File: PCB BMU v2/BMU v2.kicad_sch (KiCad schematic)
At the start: 32 parts, among them J11 Screw_Terminal_01x01, J12 Screw_Terminal_01x01, J3 Conn_01x02_Pin, U8 VPS8505, U9 MCP16331T-E/CH

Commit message: update code
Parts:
- removed JP1: SolderJumper_2_Open, Jumper:SolderJumper-2_P1.3mm_Open_RoundedPad1.0x1.5mm, symbol Jumper:SolderJumper_2_Open
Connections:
- net GND_BATT is gone; now on net GND: C12.2, C13.2, C19.2, C20.2, D1.2 (A), R25.2, U9.2 (GND)
- net batteries1/-BATT OUT is gone; now on net GND: H11.1, J12.1 (Pin_1)
- net VCC: now also U8.5 (EN)
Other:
- sheet batteries1 ports: added +BATT OUT; removed +BATT_OUT, -BATT OUT, GND_BATT
- sheet batteries2 ports: added +BATT OUT; removed +BATT_OUT, -BATT OUT
- sheet batteries3 ports: added +BATT OUT; removed +BATT_OUT, -BATT OUT
- sheet batteries4 ports: added +BATT OUT; removed +BATT_OUT, -BATT OUT
- moved on the sheet: H12, U8

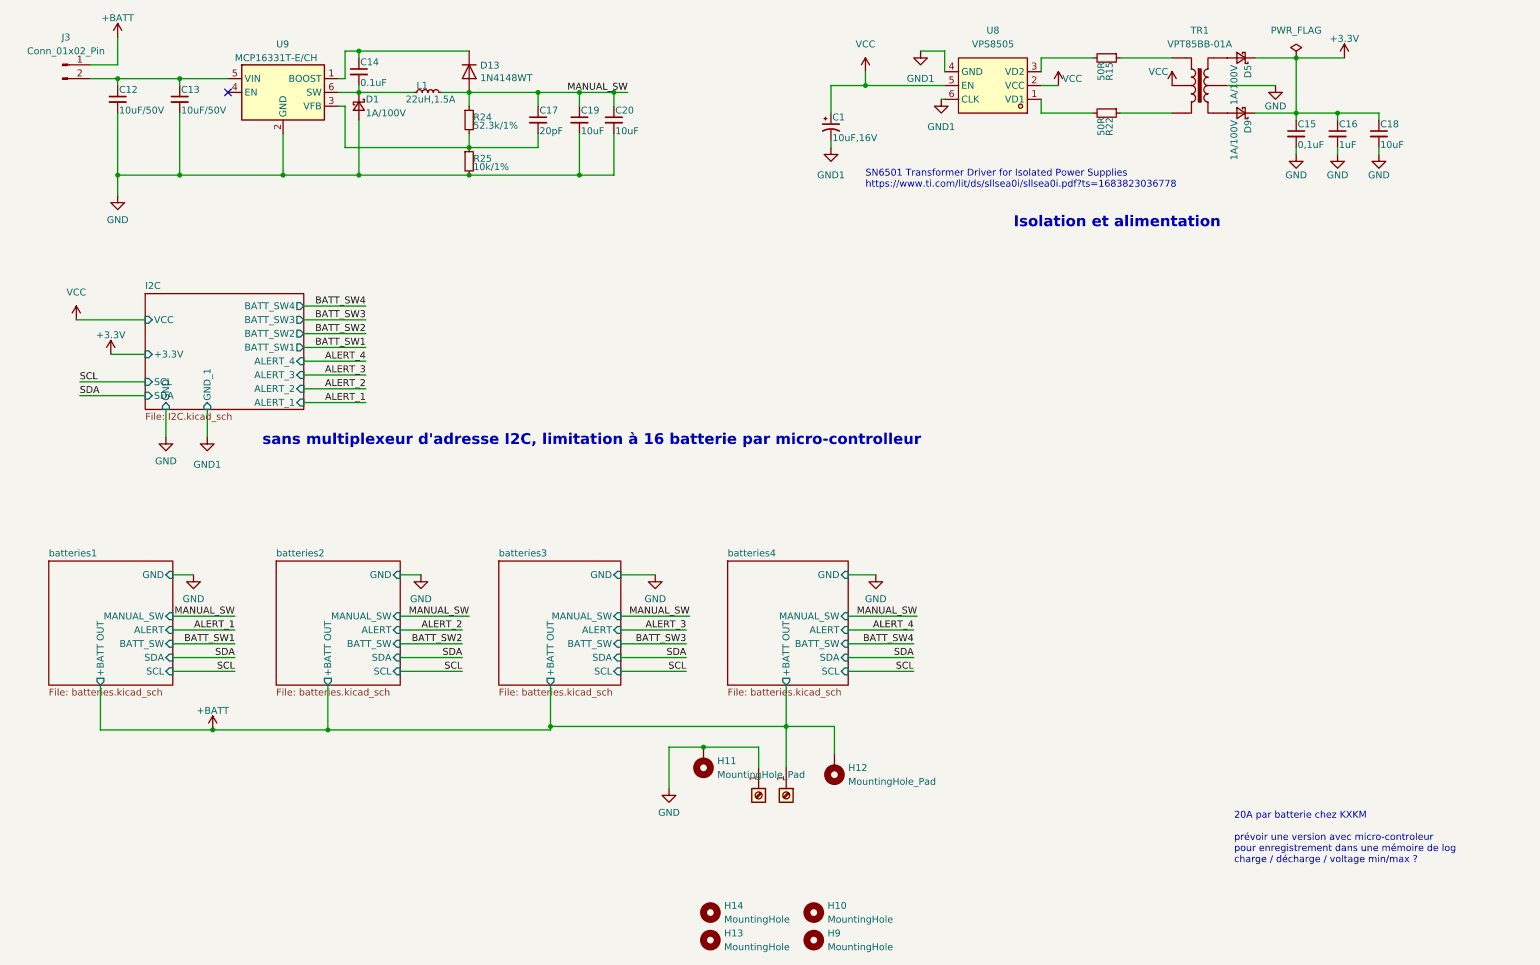
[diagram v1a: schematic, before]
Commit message: add Ampère/Houre calculation
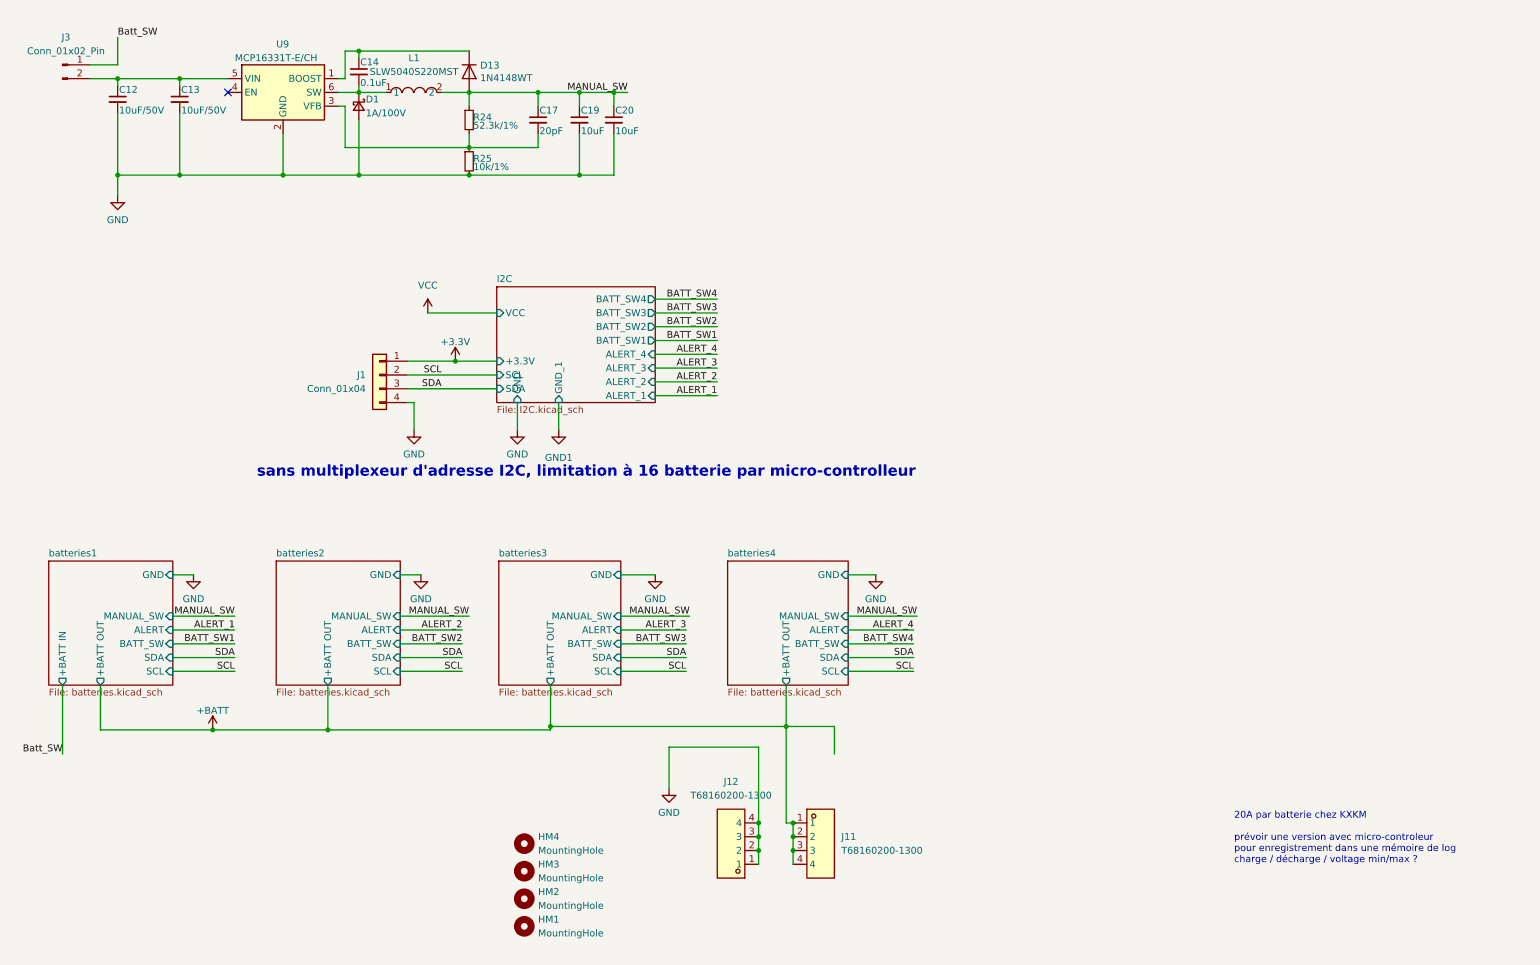
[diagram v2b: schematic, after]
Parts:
- removed C1: 10uF,16V, Capacitor_SMD:CP_Elec_8x10, symbol KXKM_ESP32_battery_management_board-rescue:CP1_Small-Device
- removed C15: 0,1uF, Capacitor_SMD:C_0805_2012Metric, symbol Device:C_Small
- removed C16: 1uF, Capacitor_SMD:C_0805_2012Metric, symbol Device:C_Small
- removed C18: 10uF, Capacitor_SMD:C_0805_2012Metric, symbol Device:C_Small
- removed D5, D9: 1A/100V, Diode_SMD:D_SMA, symbol Device:D_Schottky_Small
- removed H10, H13, H14: MountingHole, MountingHole:MountingHole_3.2mm_M3_DIN965, symbol Mechanical:MountingHole
- removed H11, H12: MountingHole_Pad, MountingHole:MountingHole_3.2mm_M3_Pad_Via, symbol Mechanical:MountingHole_Pad
- removed J11, J12: Screw_Terminal_01x01, easyeda2kicad:TH-8_L20.0-W16.0-P5.60_AMT0860001TA0000G, symbol Connector:Screw_Terminal_01x01
- removed L1: 22uH,1.5A, Inductor_SMD:L_Taiyo-Yuden_NR-50xx, symbol Device:L_Small
- removed R15, R22: 50R, Resistor_SMD:R_0603_1608Metric, symbol Device:R_Small
- removed TR1: VPT85BB-01A, Transformer_SMD:VP85BB-01A, symbol Transformer:TRANSF5
- removed U8: VPS8505, easyeda2kicad:SOT-23-6_L2.9-W1.6-P0.95-LS2.8-BR, symbol easyeda2kicad:VPS8505
- added HM2, HM3, HM4: MountingHole, MountingHole:MountingHole_2.7mm_M2.5, symbol Mechanical:MountingHole
- added J1: Conn_01x04, Connector_PinSocket_2.54mm:PinSocket_1x04_P2.54mm_Vertical, symbol Connector_Generic:Conn_01x04
- added J11, J12: T68160200-1300, easyeda2kicad:TH-8_L20.0-W16.0-P5.60_AMT0860001TA0000G, symbol easyeda2kicad:T68160200-1300
- added L1: SLW5040S220MST, easyeda2kicad:IND-SMD_L5.0-W5.0, symbol easyeda2kicad:SLW5040S220MST
- HM1: renamed from H9; footprint MountingHole:MountingHole_3.2mm_M3_DIN965 -> MountingHole:MountingHole_2.7mm_M2.5
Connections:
- net +3.3V: now also J1.1 (Pin_1)
- net +BATT: now also J11.1, J11.2, J11.3, J11.4; no longer J3.1 (Pin_1)
- net GND: now also J1.4 (Pin_4), J12.1, J12.2, J12.3, J12.4
- net MANUAL_SW: now also L1.2
- net SCL: now also J1.2 (Pin_2)
- net SDA: now also J1.3 (Pin_3)
- net at C14.2, D1.1 (K), U9.6 (SW): now also L1.1
- new net Batt_SW: J3.1 (Pin_1)
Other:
- sheet batteries1 ports: added +BATT IN; removed none
- note removed: "Isolation et alimentation"
- note removed: "SN6501 Transformer Driver for Isolated Power Supplies https://www.ti.com/lit/ds/sllsea0i/sllsea0i.pdf?ts=1683823036778"
- moved on the sheet: HM1
